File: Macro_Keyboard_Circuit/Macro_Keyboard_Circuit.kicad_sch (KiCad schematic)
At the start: 49 parts, among them J1 OSTTC082162, J2 PRT-16766, SW1 SW_Push, SW10 SW_Push, SW11 SW_Push, SW12 SW_Push, SW2 SW_Push, SW3 SW_Push, SW4 SW_Push, SW5 SW_Push, SW6 SW_Push, SW7 SW_Push, SW8 SW_Push, SW9 SW_Push, U1 KY-040, U2 Adafruit KB2040, U3 KY-040, U4 KY-040

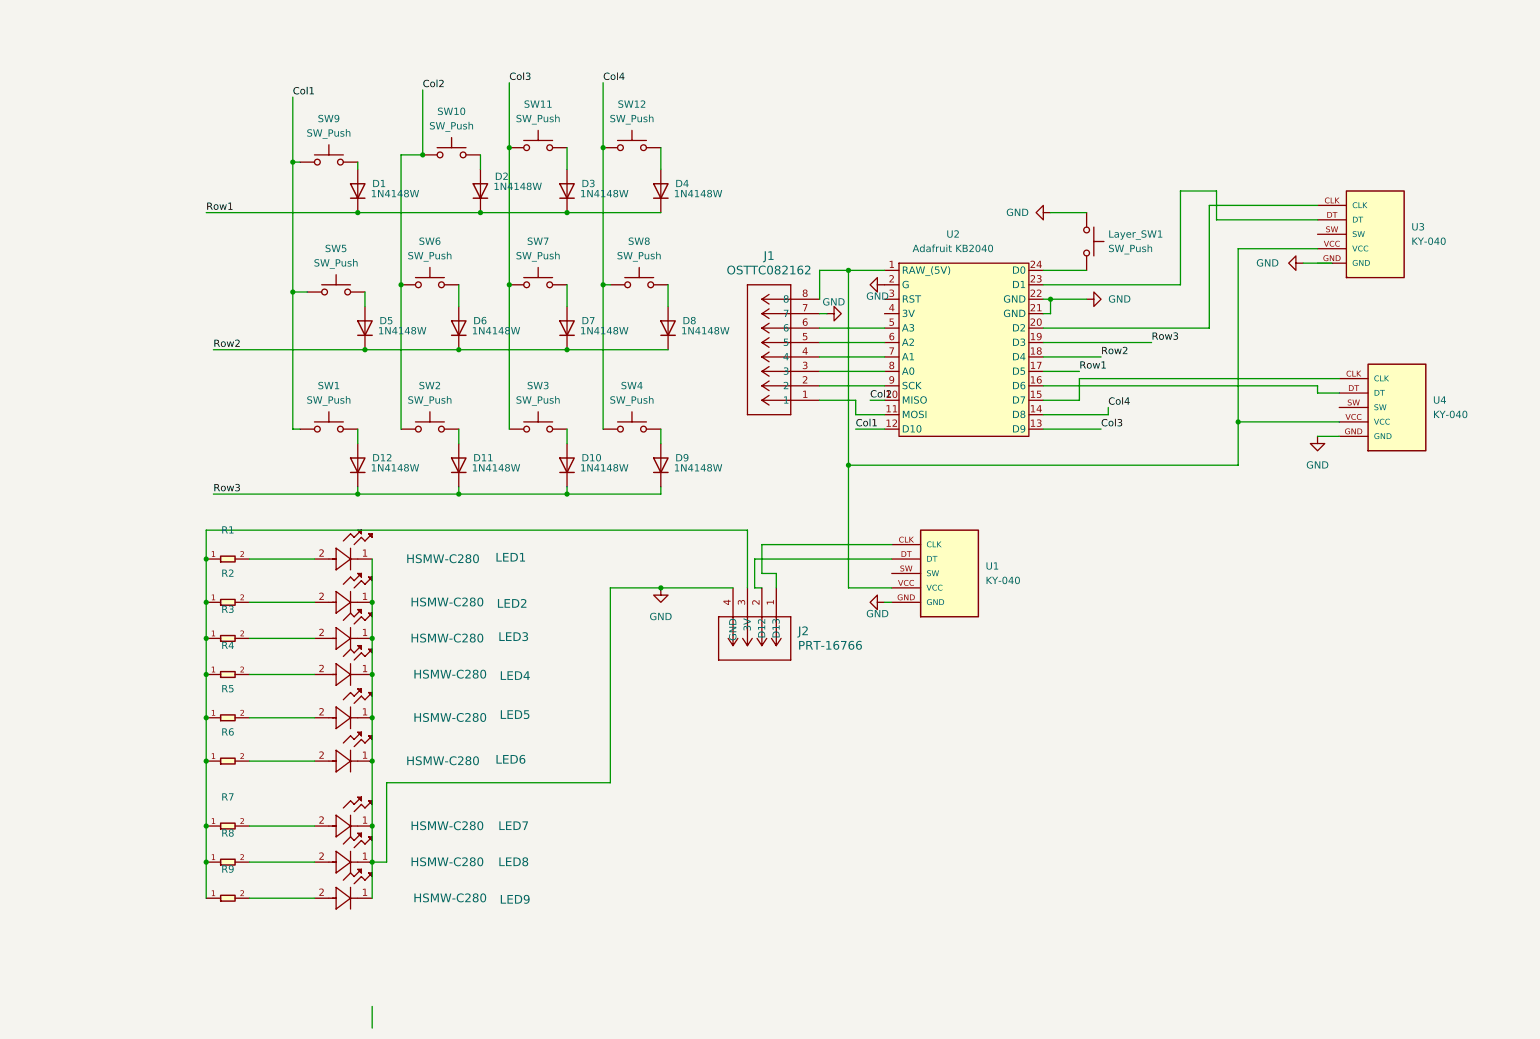
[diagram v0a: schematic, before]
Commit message: Major revision to circuit due to change in acess to assembly tools. Finalized verson of PCB. Still need to update board codebase to reflect the new board configurations.
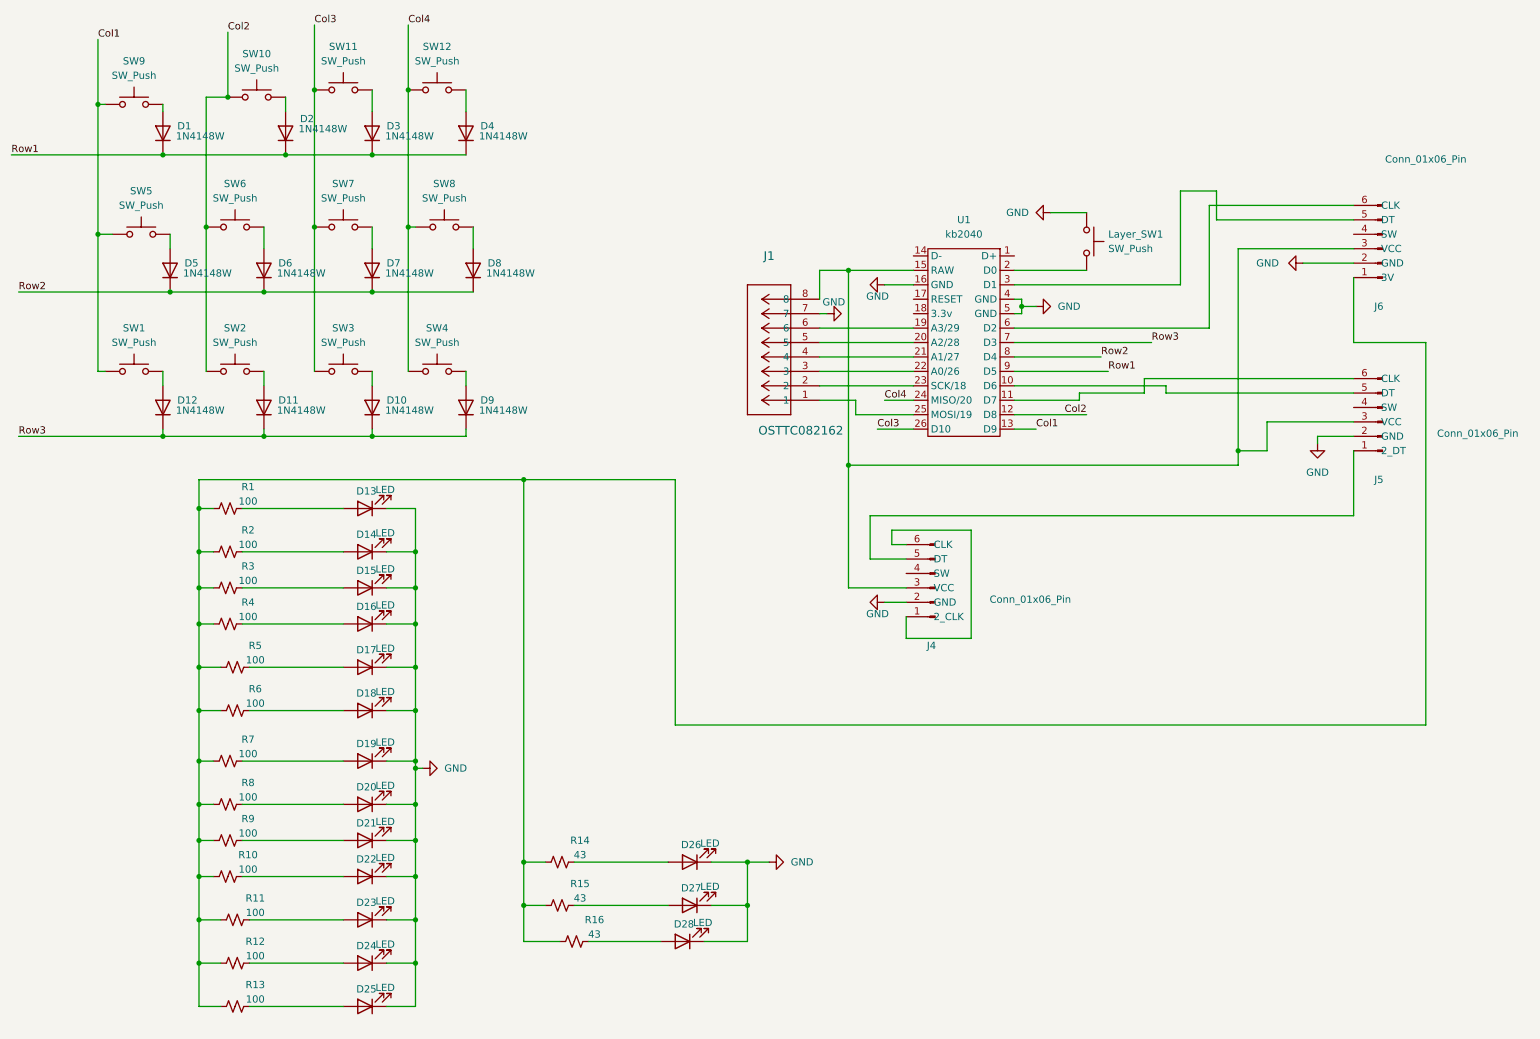
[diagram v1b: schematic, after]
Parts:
- removed J2: PRT-16766, PRT_16766:CONN_BM04B-SRSS-TB_SPK, symbol PRT_16766:PRT-16766
- removed LED1, LED2, LED3, LED4, LED5, LED6, LED7, LED8, LED9: HSMW-C280, HSMW_C280:LED_HSMW-C280_BRA, symbol HSMW_C280:HSMW-C280
- removed R1, R2, R3, R4, R5, R6, R7, R8, R9: 33R, RC0402FR-0733RL:R0402, symbol RC0402FR-0733RL:SMD-RES-33R-1_-1_16W_0402_
- removed U1, U3, U4: KY-040, KY_040:KY_040_PORT, symbol KY-040:KY-040
- removed U2: Adafruit KB2040, SparkFun-Board:ProMicroC, symbol SparkFun-Board:ProMicroC
- added D13, D14, D15, D16, D17, D18, D19, D20, D21, D22, D23, D24, D25: LED, SW_Cherry_MX:D_0603_1608Metric_Pad1.05x0.95mm_HandSolder_cherrymx_silk, symbol Device:LED
- added D26, D27, D28: LED, Diode_THT:D_A-405_P2.54mm_Vertical_AnodeUp, symbol Device:LED
- added J4, J5, J6: Conn_01x06_Pin, Connector_PinHeader_2.54mm:PinHeader_1x06_P2.54mm_Vertical, symbol Connector:Conn_01x06_Pin
- added R1, R10, R11, R12, R13, R2, R3, R4, R5, R6, R7, R8, R9: 100, SparkFun-Resistor:R_0603_1608Metric, symbol SparkFun-Resistor:0_0603
- added R14, R15, R16: 43, SparkFun-Resistor:R_0603_1608Metric, symbol SparkFun-Resistor:0_0603
- added U1: kb2040, kb2040:kb2040, symbol kb2040_new:kb2040
- Layer_SW1, SW1, SW10, SW11, SW12, SW2, SW3, SW4, SW5, SW6, SW7, SW8, SW9: footprint Button_Switch_Keyboard:SW_Cherry_MX_1.00u_PCB -> SW_Cherry_MX:SW_Cherry_modified
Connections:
- net Col1: now also U1.13 (D9)
- net Col2: now also U1.12 (D8)
- net Col3: now also U1.26 (D10)
- net Col4: now also U1.24 (MISO/20)
- net GND: now also D13.1 (K), D14.1 (K), D15.1 (K), D16.1 (K), D17.1 (K), D18.1 (K), D19.1 (K), D20.1 (K), D21.1 (K), D22.1 (K), D23.1 (K), D24.1 (K), D25.1 (K), D26.1 (K), D27.1 (K), D28.1 (K), J4.2 (GND), J5.2 (GND), J6.2 (GND), U1.16 (GND), U1.4 (GND), U1.5 (GND)
- net Row1: now also U1.9 (D5)
- net Row2: now also U1.8 (D4)
- net Row3: now also U1.7 (D3)
- net at J1.8: now also J4.3 (VCC), J5.3 (VCC), J6.3 (VCC), U1.15 (RAW)
- net at J1.1: now also U1.25 (MOSI/19)
- net at Layer_SW1.2: now also U1.2 (D0)
- net at J1.6: now also U1.19 (A3/29)
- net at J1.5: now also U1.20 (A2/28)
- net at J1.4: now also U1.21 (A1/27)
- net at J1.3: now also U1.22 (A0/26)
- net at J1.2: now also U1.23 (SCK/18)
- new net: J6.1 (3V), R1.1, R10.1, R11.1, R12.1, R13.1, R14.1, R15.1, R16.1, R2.1, R3.1, R4.1, R5.1, R6.1, R7.1, R8.1, R9.1
- new net: D13.2 (A), R1.2
- new net: D19.2 (A), R7.2
- new net: J4.5 (DT), J5.1 (2_DT)
- new net: J5.5 (DT), U1.10 (D6)
- new net: J5.6 (CLK), U1.11 (D7)
- new net: J6.5 (DT), U1.3 (D1)
- new net: J6.6 (CLK), U1.6 (D2)
- new net: D17.2 (A), R5.2
- new net: D26.2 (A), R14.2
- new net: D16.2 (A), R4.2
- new net: D21.2 (A), R9.2
- new net: D25.2 (A), R13.2
- new net: D27.2 (A), R15.2
- new net: D22.2 (A), R10.2
- new net: D23.2 (A), R11.2
- new net: D20.2 (A), R8.2
- new net: D14.2 (A), R2.2
- new net: D24.2 (A), R12.2
- new net: D18.2 (A), R6.2
- new net: D15.2 (A), R3.2
- new net: D28.2 (A), R16.2
- new net: J4.1 (2_CLK), J4.6 (CLK)
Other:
- moved on the sheet: D1, D10, D11, D12, D2, D3, D4, D5, D6, D7, D8, D9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
